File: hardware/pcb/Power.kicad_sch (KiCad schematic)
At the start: 14 parts, among them J4 USB_B_Micro, SW1 CSS-1210TB, U3 MCP73831-2-OT, U4 RN4989, U5 NCP160AMX330TBG

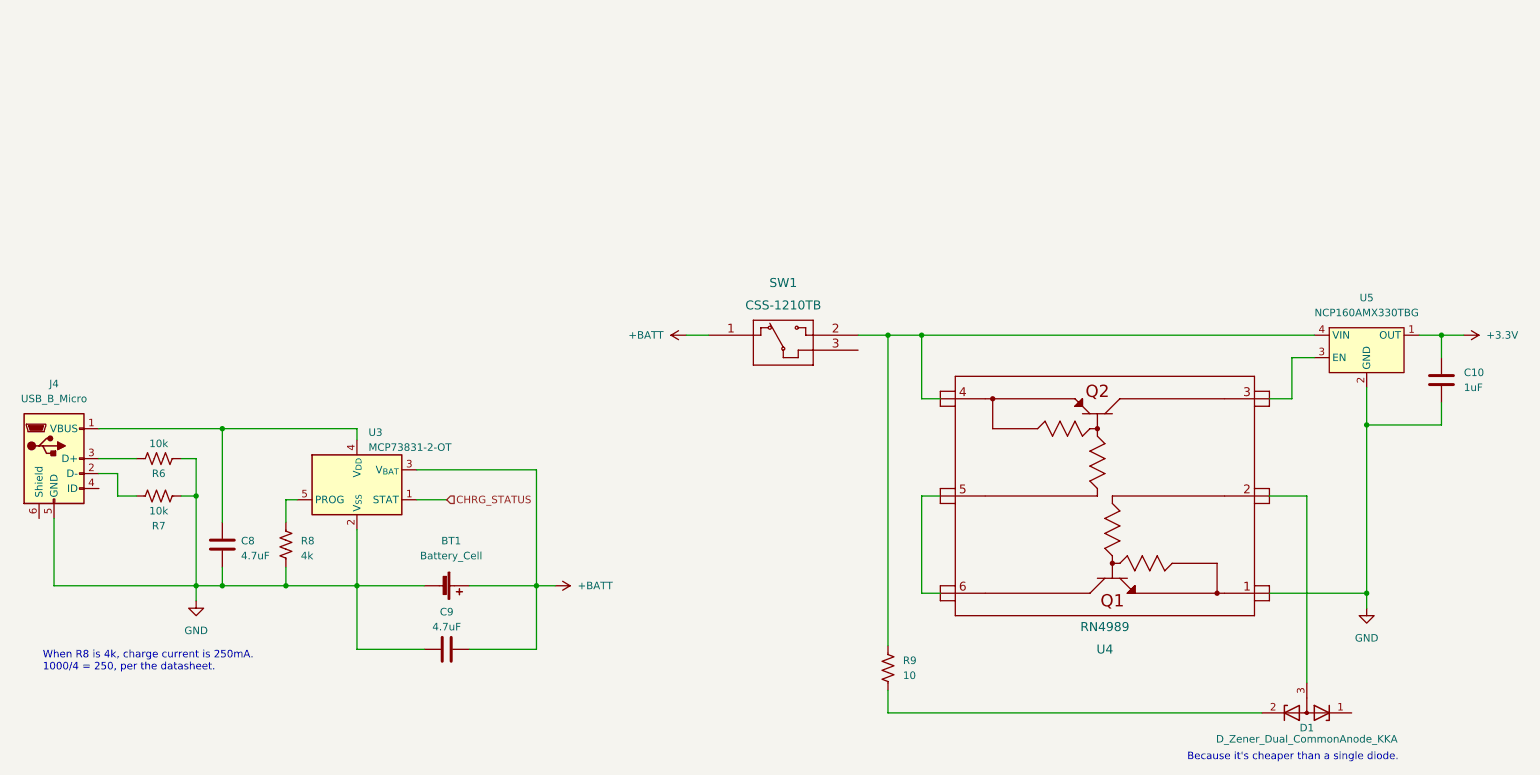
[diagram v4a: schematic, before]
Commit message: Replace zener diode setup with TLV431
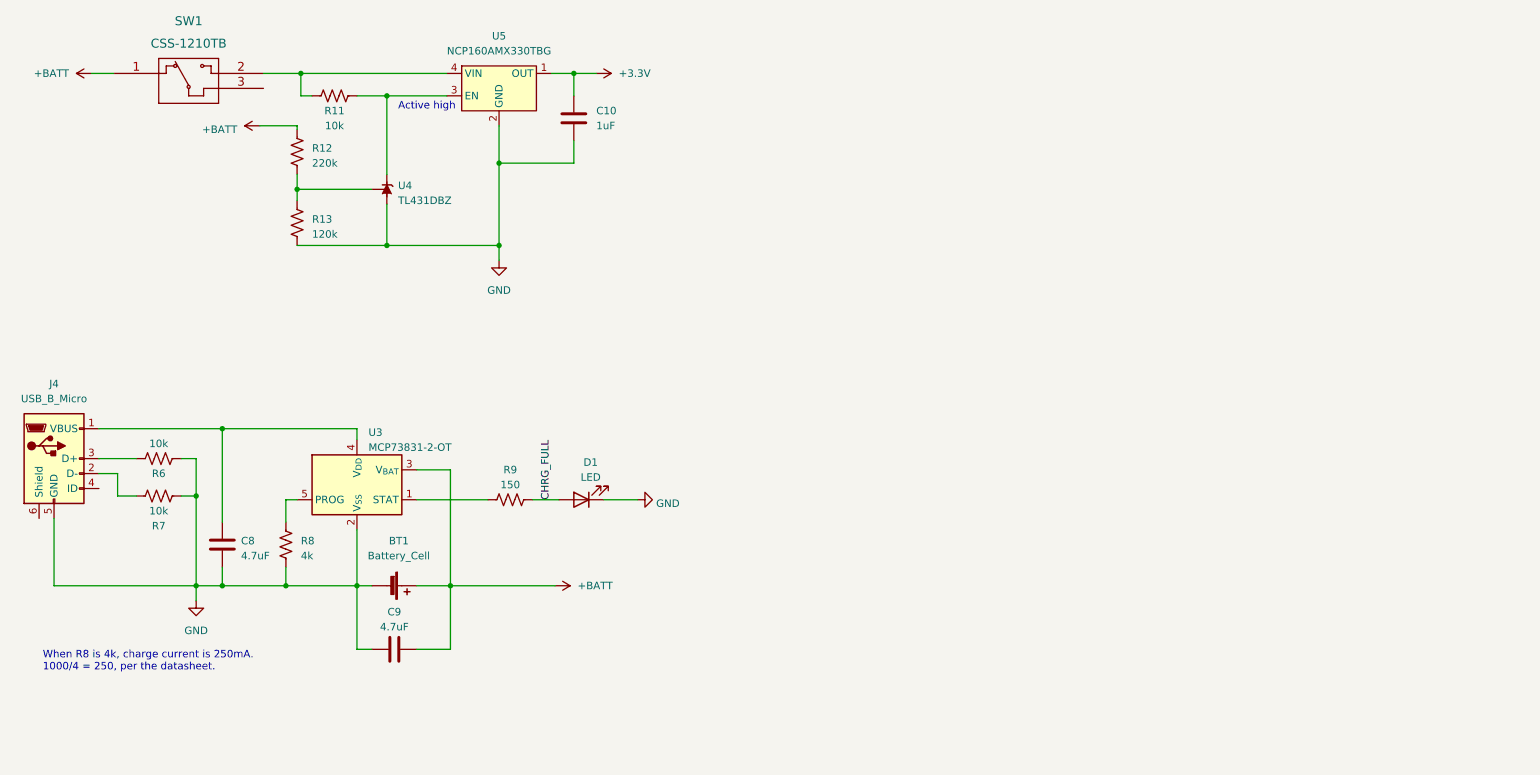
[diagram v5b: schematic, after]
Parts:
- removed D1: D_Zener_Dual_CommonAnode_KKA, Package_TO_SOT_SMD:SOT-23, symbol Device:D_Zener_Dual_CommonAnode_KKA
- removed U4: RN4989, RN4989:RN4989, symbol RN4989:RN4989
- added D1: LED, LED_SMD:LED_1206_3216Metric_Pad1.42x1.75mm_HandSolder, symbol Device:LED
- added R11: 10k, Resistor_SMD:R_0805_2012Metric_Pad1.20x1.40mm_HandSolder, symbol Device:R_US
- added R12: 220k, Resistor_SMD:R_0805_2012Metric_Pad1.20x1.40mm_HandSolder, symbol Device:R_US
- added R13: 120k, Resistor_SMD:R_0805_2012Metric_Pad1.20x1.40mm_HandSolder, symbol Device:R_US
- added U4: TL431DBZ, Package_TO_SOT_SMD:SOT-23, symbol Reference_Voltage:TL431DBZ
- R9: value 10 -> 150; footprint Resistor_SMD:R_1206_3216Metric_Pad1.30x1.75mm_HandSolder -> Resistor_SMD:R_0805_2012Metric_Pad1.20x1.40mm_HandSolder
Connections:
- net +BATT: now also R12.2
- net GND: now also D1.1 (K), R13.1, U4.3 (A)
- net at SW1.2, U5.4 (VIN): now also R11.1; no longer R9.1
- net at U5.3 (EN): now also R11.2, U4.1 (K)
- net CHRG_FULL: now reaches R9.2
- net CHRG_FULL: now also D1.2 (A)
- net CHRG_STATUS: no longer names the net of U3.1 (STAT)
- net CHRG_STATUS: now also R9.1
- new net: R12.1, R13.2, U4.2 (REF)
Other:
- note added: "Active high"
- note removed: "Because it's cheaper than a single diode."
- moved on the sheet: BT1, C10, C9, SW1, U5

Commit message: Make all resistors 1206 and LEDs 0805
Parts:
- D1: footprint LED_SMD:LED_1206_3216Metric_Pad1.42x1.75mm_HandSolder -> LED_SMD:LED_0805_2012Metric_Pad1.15x1.40mm_HandSolder
- R11, R12, R13, R9: footprint Resistor_SMD:R_0805_2012Metric_Pad1.20x1.40mm_HandSolder -> Resistor_SMD:R_1206_3216Metric_Pad1.30x1.75mm_HandSolder
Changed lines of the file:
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@@
       (effects (font (size 1.27 1.27)) (justify right))
     )
-    (property "Footprint" "Resistor_SMD:R_0805_2012Metric_Pad1.20x1.40mm_HandSolder" (at 65.024 51.816 90)
+    (property "Footprint" "Resistor_SMD:R_1206_3216Metric_Pad1.30x1.75mm_HandSolder" (at 65.024 51.816 90)
       (effects (font (size 1.27 1.27)) hide)
     )
@@
       (effects (font (size 1.27 1.27)) (justify right))
     )
-    (property "Footprint" "Resistor_SMD:R_0805_2012Metric_Pad1.20x1.40mm_HandSolder" (at 65.024 39.751 90)
+    (property "Footprint" "Resistor_SMD:R_1206_3216Metric_Pad1.30x1.75mm_HandSolder" (at 65.024 39.751 90)
       (effects (font (size 1.27 1.27)) hide)
     )
@@
       (effects (font (size 1.27 1.27)))
     )
-    (property "Footprint" "Resistor_SMD:R_0805_2012Metric_Pad1.20x1.40mm_HandSolder" (at 72.644 29.464 90)
+    (property "Footprint" "Resistor_SMD:R_1206_3216Metric_Pad1.30x1.75mm_HandSolder" (at 72.644 29.464 90)
       (effects (font (size 1.27 1.27)) hide)
     )
@@
       (effects (font (size 1.27 1.27)))
     )
-    (property "Footprint" "LED_SMD:LED_1206_3216Metric_Pad1.42x1.75mm_HandSolder" (at 114.3 99.06 0)
+    (property "Footprint" "LED_SMD:LED_0805_2012Metric_Pad1.15x1.40mm_HandSolder" (at 114.3 99.06 0)
       (effects (font (size 1.27 1.27)) hide)
     )
@@
       (effects (font (size 1.27 1.27)))
     )
-    (property "Footprint" "Resistor_SMD:R_0805_2012Metric_Pad1.20x1.40mm_HandSolder" (at 102.489 98.044 90)
-      (effects (font (size 1.27 1.27)) hide)
-    )
+    (property "Footprint" "Resistor_SMD:R_1206_3216Metric_Pad1.30x1.75mm_HandSolder" (at 102.489 98.044 90)
+      (effects (font (size 1.27 1.27)) hide)
+    )

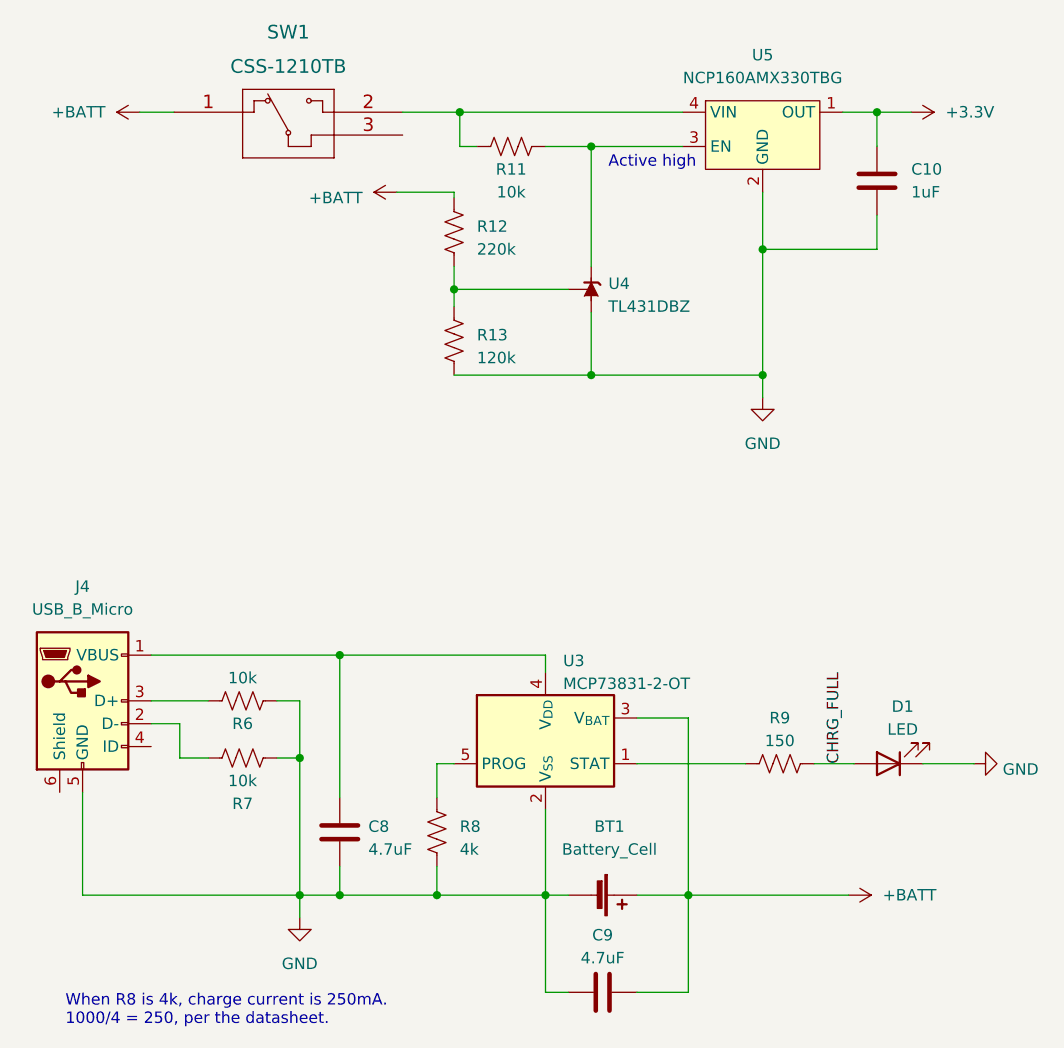
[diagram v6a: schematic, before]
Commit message: Switch to TLV4333PDBVR LDO regulator
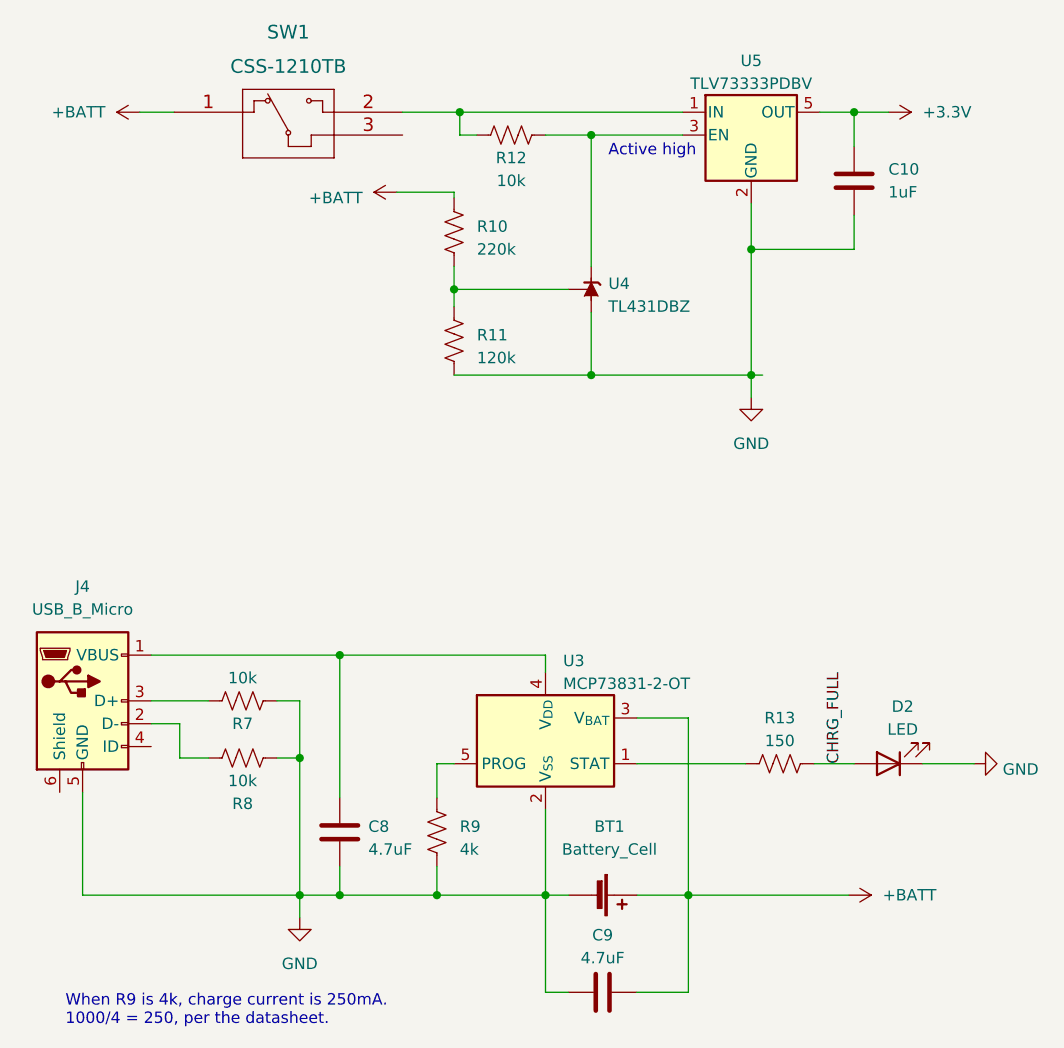
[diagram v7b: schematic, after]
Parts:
- removed U5: NCP160AMX330TBG, Package_DFN_QFN:OnSemi_XDFN4-1EP_1.0x1.0mm_EP0.52x0.52mm, symbol NCP160:NCP160AMX330TBG
- added U5: TLV73333PDBV, Package_TO_SOT_SMD:SOT-23-5, symbol Regulator_Linear:TLV73333PDBV
- renumbered D1 to D2, R12 to R10, R13 to R11, R11 to R12, R9 to R13, R6 to R7, R7 to R8, R8 to R9
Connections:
- net +3.3V: now also U5.5 (OUT)
- net GND: now also U5.2 (GND)
- net at R12.1, SW1.2: now also U5.1 (IN)
- net at R12.2, U4.1 (K): now also U5.3 (EN)
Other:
- note added: "When R9 is 4k, charge current is 250mA. 1000/4 = 250, per the datasheet."
- note removed: "When R8 is 4k, charge current is 250mA. 1000/4 = 250, per the datasheet."
- moved on the sheet: C10, R12

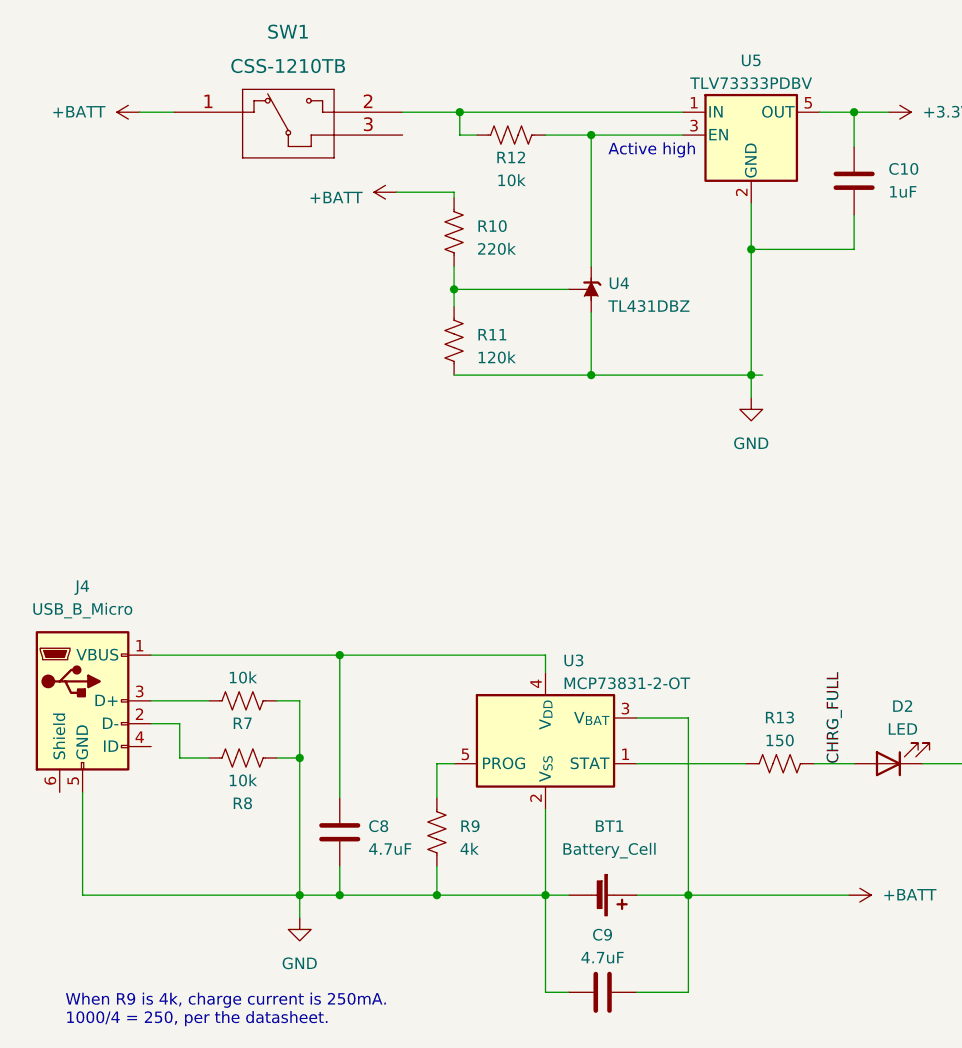
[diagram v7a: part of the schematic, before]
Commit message: Replace BGA IC with QFN
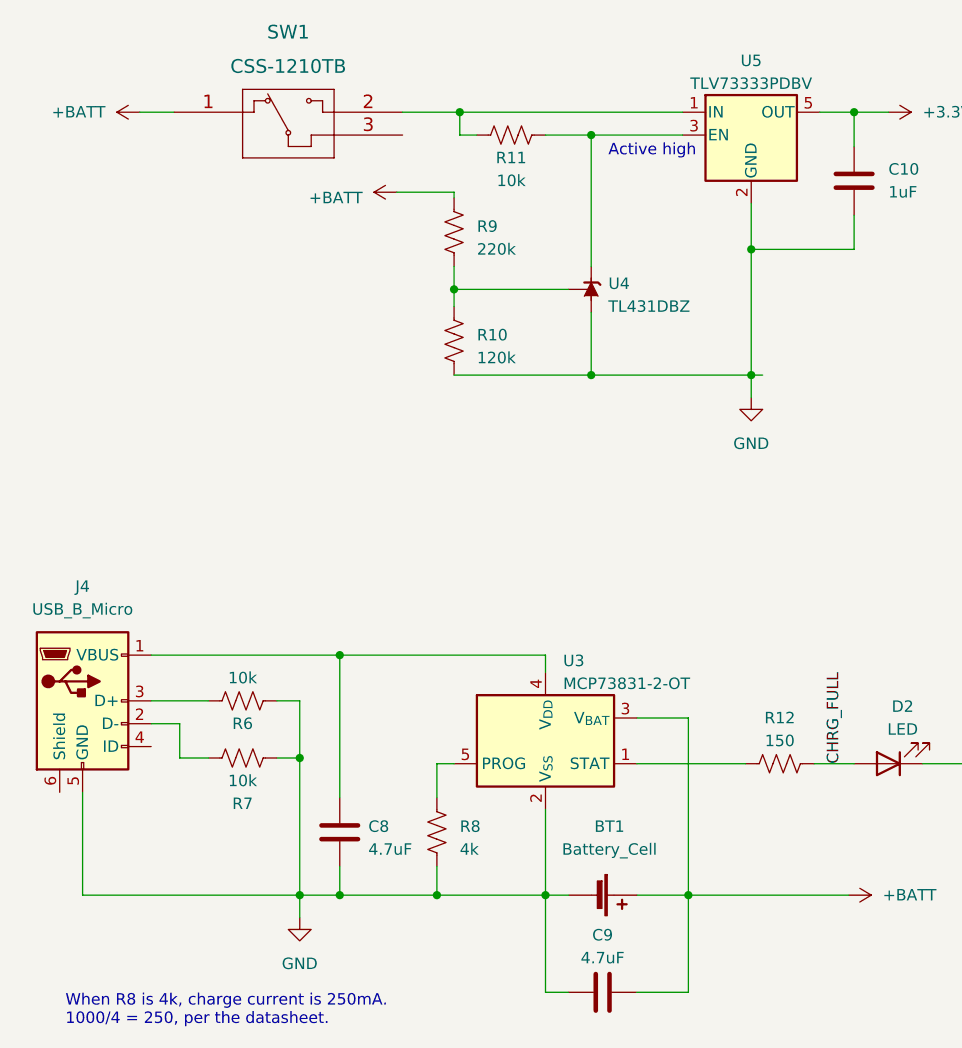
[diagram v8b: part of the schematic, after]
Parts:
- renumbered R11 to R10, R12 to R11, R13 to R12, R7 to R6, R8 to R7, R9 to R8, R10 to R9
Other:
- note added: "When R8 is 4k, charge current is 250mA. 1000/4 = 250, per the datasheet."
- note removed: "When R9 is 4k, charge current is 250mA. 1000/4 = 250, per the datasheet."
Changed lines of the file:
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@@
     (stroke (width 0) (type default))
   )
-  (text "When R9 is 4k, charge current is 250mA.\n1000/4 = 250, per the datasheet."
+  (text "When R8 is 4k, charge current is 250mA.\n1000/4 = 250, per the datasheet."
     (at 22.86 128.27 0)
     (effects (font (size 1.27 1.27)) (justify left bottom))
@@
   (symbol (lib_id "Device:R_US") (at 66.04 52.07 180) (unit 1)
     (in_bom yes) (on_board yes) (dnp no) (fields_autoplaced)
-    (property "Reference" "R11" (at 68.58 51.435 0)
+    (property "Reference" "R10" (at 68.58 51.435 0)
       (effects (font (size 1.27 1.27)) (justify right))
     )
@@
       (project "Combadge"
         (path "/dc42e7bc-f663-434d-8744-232038ac4fdf/522738f4-f6b2-4897-a079-07da122bd152"
-          (reference "R11") (unit 1)
+          (reference "R10") (unit 1)
         )
       )
@@
   (symbol (lib_id "Device:R_US") (at 64.135 106.68 0) (unit 1)
     (in_bom yes) (on_board yes) (dnp no) (fields_autoplaced)
-    (property "Reference" "R9" (at 66.675 106.045 0)
+    (property "Reference" "R8" (at 66.675 106.045 0)
       (effects (font (size 1.27 1.27)) (justify left))
     )
@@
       (project "Combadge"
         (path "/dc42e7bc-f663-434d-8744-232038ac4fdf/522738f4-f6b2-4897-a079-07da122bd152"
-          (reference "R9") (unit 1)
+          (reference "R8") (unit 1)
         )
       )
@@
   (symbol (lib_id "Device:R_US") (at 66.04 40.005 180) (unit 1)
     (in_bom yes) (on_board yes) (dnp no) (fields_autoplaced)
-    (property "Reference" "R10" (at 68.58 39.37 0)
+    (property "Reference" "R9" (at 68.58 39.37 0)
       (effects (font (size 1.27 1.27)) (justify right))
     )
@@
       (project "Combadge"
         (path "/dc42e7bc-f663-434d-8744-232038ac4fdf/522738f4-f6b2-4897-a079-07da122bd152"
-          (reference "R10") (unit 1)
+          (reference "R9") (unit 1)
         )
       )
@@
   (symbol (lib_id "Device:R_US") (at 72.39 29.21 90) (unit 1)
     (in_bom yes) (on_board yes) (dnp no)
-    (property "Reference" "R12" (at 72.39 31.75 90)
+    (property "Reference" "R11" (at 72.39 31.75 90)
       (effects (font (size 1.27 1.27)))
     )
@@
       (project "Combadge"
         (path "/dc42e7bc-f663-434d-8744-232038ac4fdf/522738f4-f6b2-4897-a079-07da122bd152"
-          (reference "R12") (unit 1)
+          (reference "R11") (unit 1)
         )
       )
@@
   (symbol (lib_id "Device:R_US") (at 42.545 92.075 90) (unit 1)
     (in_bom yes) (on_board yes) (dnp no)
-    (property "Reference" "R7" (at 42.545 94.615 90)
+    (property "Reference" "R6" (at 42.545 94.615 90)
       (effects (font (size 1.27 1.27)))
     )
@@
       (project "Combadge"
         (path "/dc42e7bc-f663-434d-8744-232038ac4fdf/522738f4-f6b2-4897-a079-07da122bd152"
-          (reference "R7") (unit 1)
+          (reference "R6") (unit 1)
         )
       )
@@
   (symbol (lib_id "Device:R_US") (at 102.235 99.06 90) (unit 1)
     (in_bom yes) (on_board yes) (dnp no) (fields_autoplaced)
-    (property "Reference" "R13" (at 102.235 93.98 90)
+    (property "Reference" "R12" (at 102.235 93.98 90)
       (effects (font (size 1.27 1.27)))
     )
@@
       (project "Combadge"
         (path "/dc42e7bc-f663-434d-8744-232038ac4fdf/522738f4-f6b2-4897-a079-07da122bd152"
-          (reference "R13") (unit 1)
+          (reference "R12") (unit 1)
         )
       )
@@
   (symbol (lib_id "Device:R_US") (at 42.545 98.425 90) (unit 1)
     (in_bom yes) (on_board yes) (dnp no)
-    (property "Reference" "R8" (at 42.545 103.505 90)
+    (property "Reference" "R7" (at 42.545 103.505 90)
       (effects (font (size 1.27 1.27)))
     )
@@
       (project "Combadge"
         (path "/dc42e7bc-f663-434d-8744-232038ac4fdf/522738f4-f6b2-4897-a079-07da122bd152"
-          (reference "R8") (unit 1)
-        )
-      )
+          (reference "R7") (unit 1)
+        )
+      )
